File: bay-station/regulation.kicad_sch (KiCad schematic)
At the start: 7 parts, among them U8 TPS62A02PDDCR

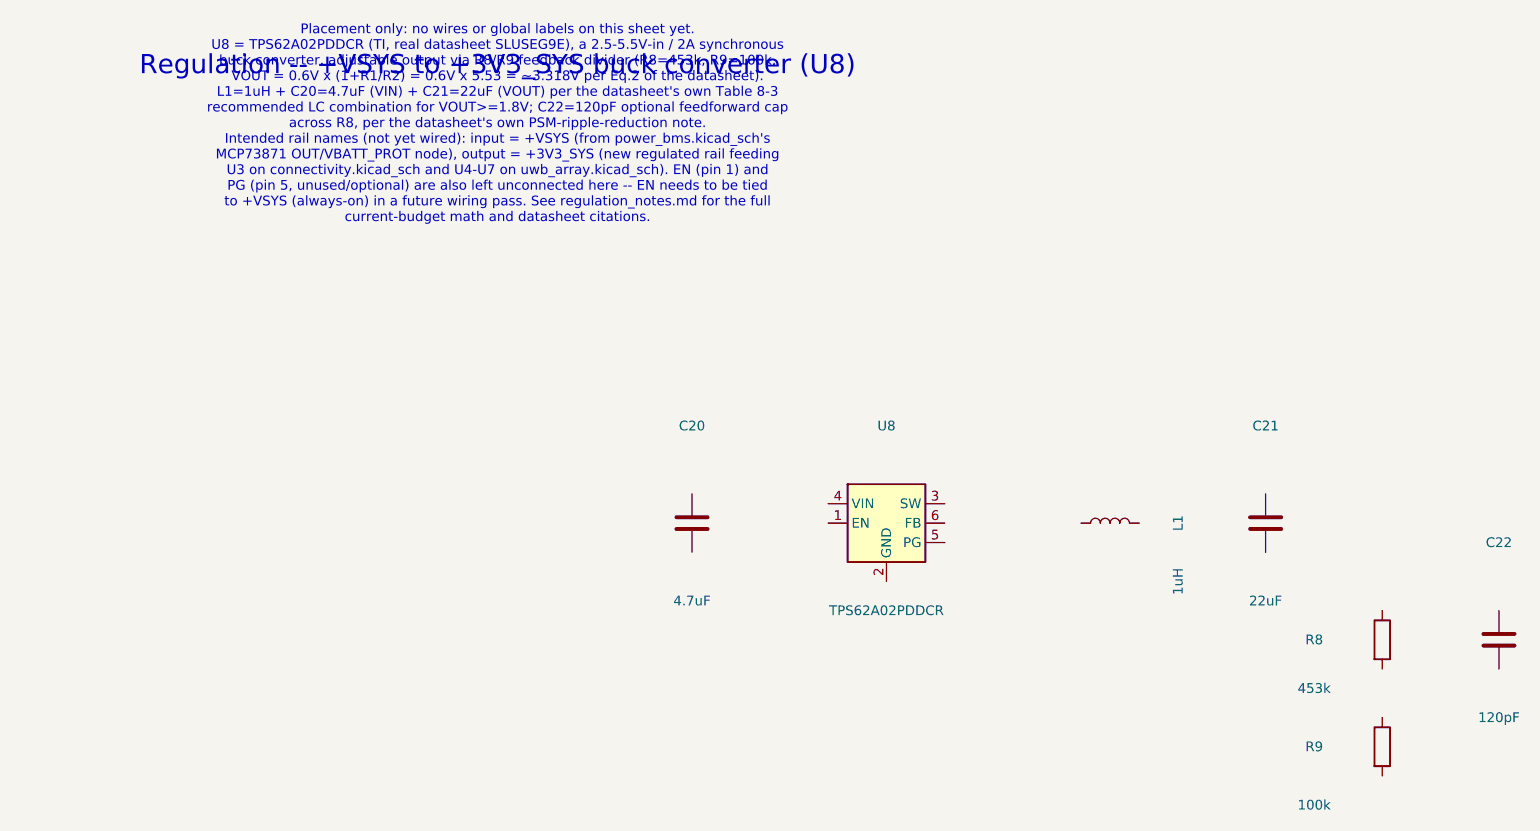
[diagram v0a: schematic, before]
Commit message: Wire up power_bms, regulation and programming_debug; tie off floating grounds
The bay station was built entirely from global labels and power symbols --
zero drawn wires on any sheet. This starts converting the power path to
explicit wiring and connects the grounds that were left floating:

- power_bms: 62 wires; 31 label justifications flipped left->right where
  the labels were mirrored. No symbols added or removed.
- regulation: 11 wires, 3 junctions, 5 GND symbols (#PWR01-05).
- programming_debug: 2 wires, 1 junction, 1 GND symbol (#PWR06).

ERC goes 518 -> 497 violations (494 -> 473 errors), entirely in
pin_not_connected (360 -> 342), power_pin_not_driven (98 -> 96) and
pin_not_driven (36 -> 35). Nothing regressed. The remaining 342
pin_not_connected are the sheets that are still label-only.

Unavoidable churn in this commit: KiCad 10 re-serialized seven sheets from
8.0 format (version 20231120) to 10.0 (20260306) on save -- clock_dist,
connectivity, gnss, indicators, programming_debug, testpoints, uwb_array.
That accounts for most of the diff; those seven have no content change
beyond it. CLAUDE.md asks that the format not be bumped as a side effect,
but it cannot be split out here: kicad-cli sch upgrade serializes
differently from the GUI and leaves ~3700 lines of residual churn, so a
format-only commit would be tidier in shape and no more honest. Four
sheets were already on 10.0 format before this commit.

Co-Authored-By: Claude Opus 5 (1M context) <noreply@anthropic.com>
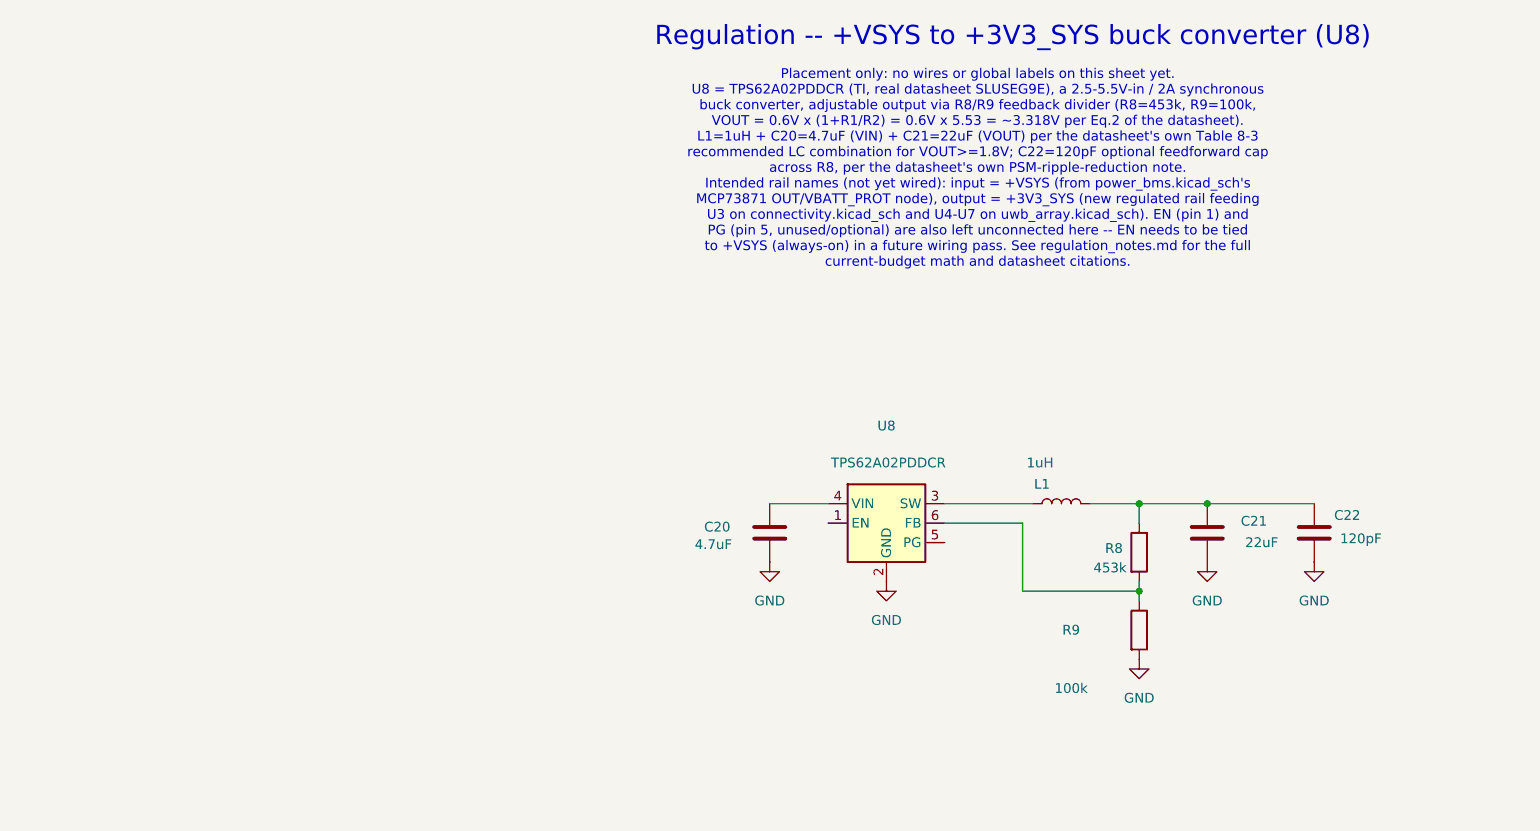
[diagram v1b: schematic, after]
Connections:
- net at R8.1: now also C21.1, C22.1, L1.2
- net at R8.2: now also R9.1, U8.6 (FB)
- net GND: now reaches R9.2
- net GND: now also C20.2, C21.2, C22.2, U8.2 (GND)
- net at L1.1: now also U8.3 (SW)
- net at U8.4 (VIN): now also C20.1
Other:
- moved on the sheet: C20, C21, C22, L1, R8, R9
